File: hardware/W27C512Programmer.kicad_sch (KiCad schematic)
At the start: 104 parts, among them J1 CTRL, J2 MSB, J3 LSB, J4 Ext_UART, J5 OLED, J6 VP, J7 SAO, Q1 MMBT3904, Q2 MMBT3906, Q3 MMBT3904, Q4 MMBT3904, Q5 MMBT3904, Q6 MMBT3906, Q7 MMBT3906, Q8 MMBT3906, SW1 RST, SW2 USR, U1 MIC2288, U2 74HC573, U3 74HC573, U4 74HC573, U5 28/32 pin ROM

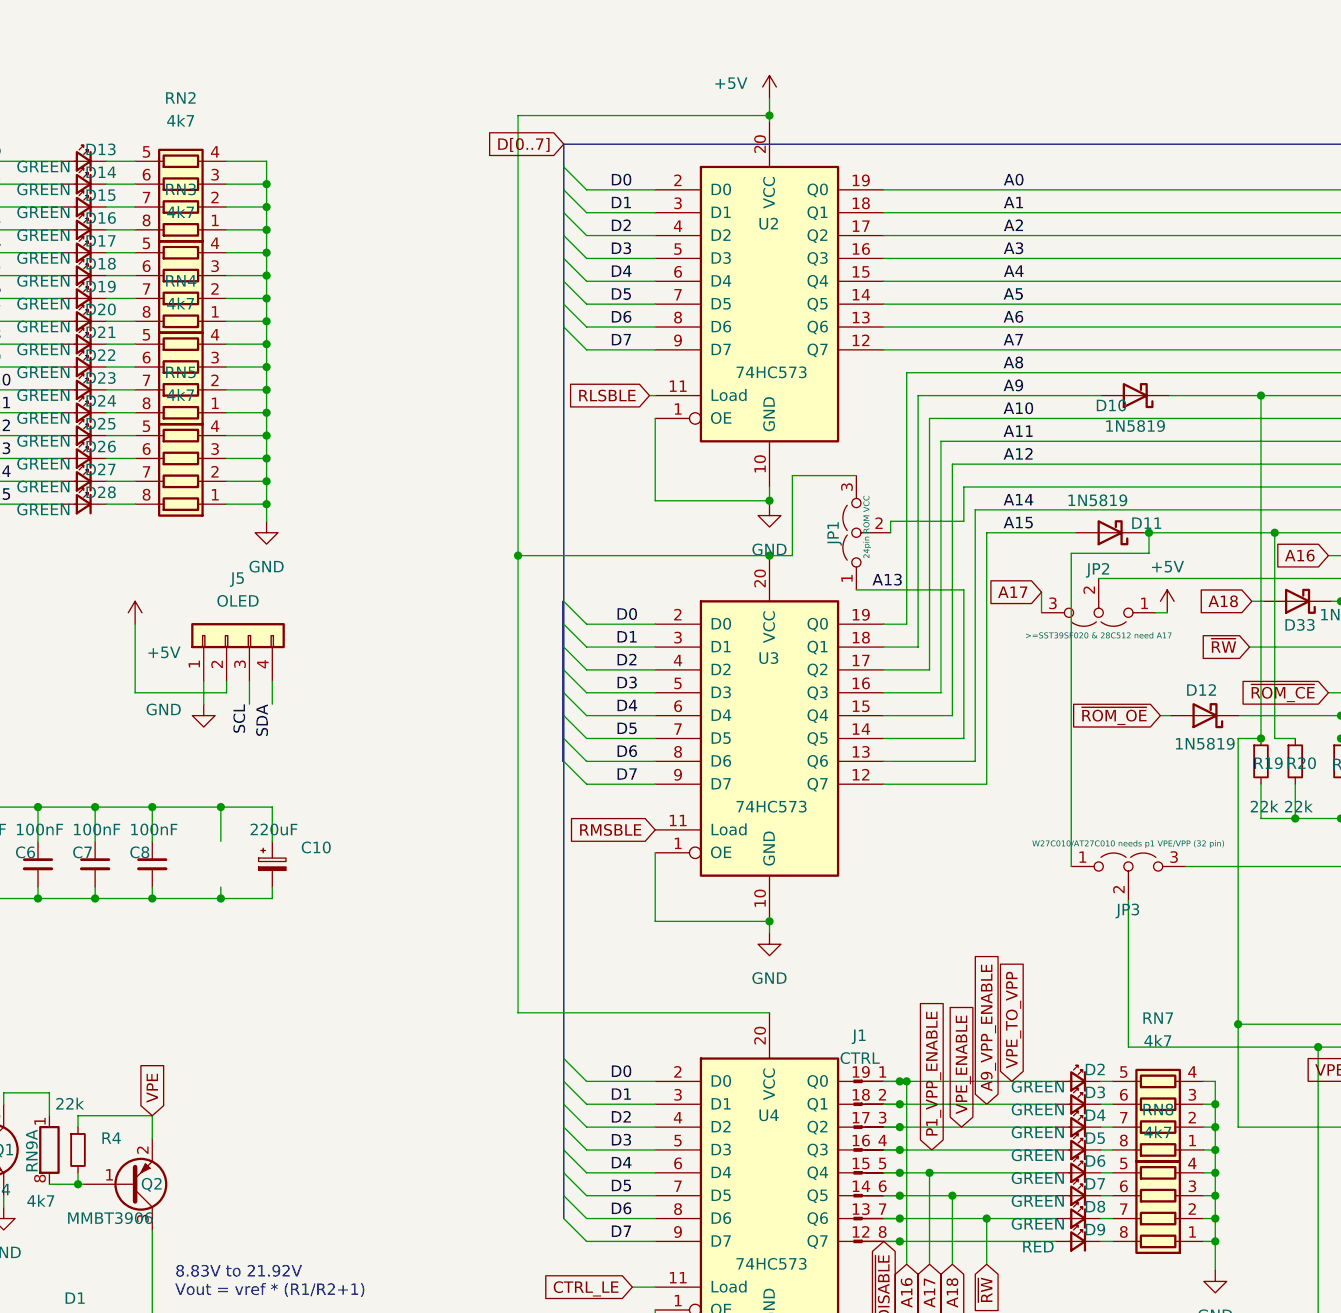
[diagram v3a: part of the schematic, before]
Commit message: Change 4k7 to 10k R for green LEDs
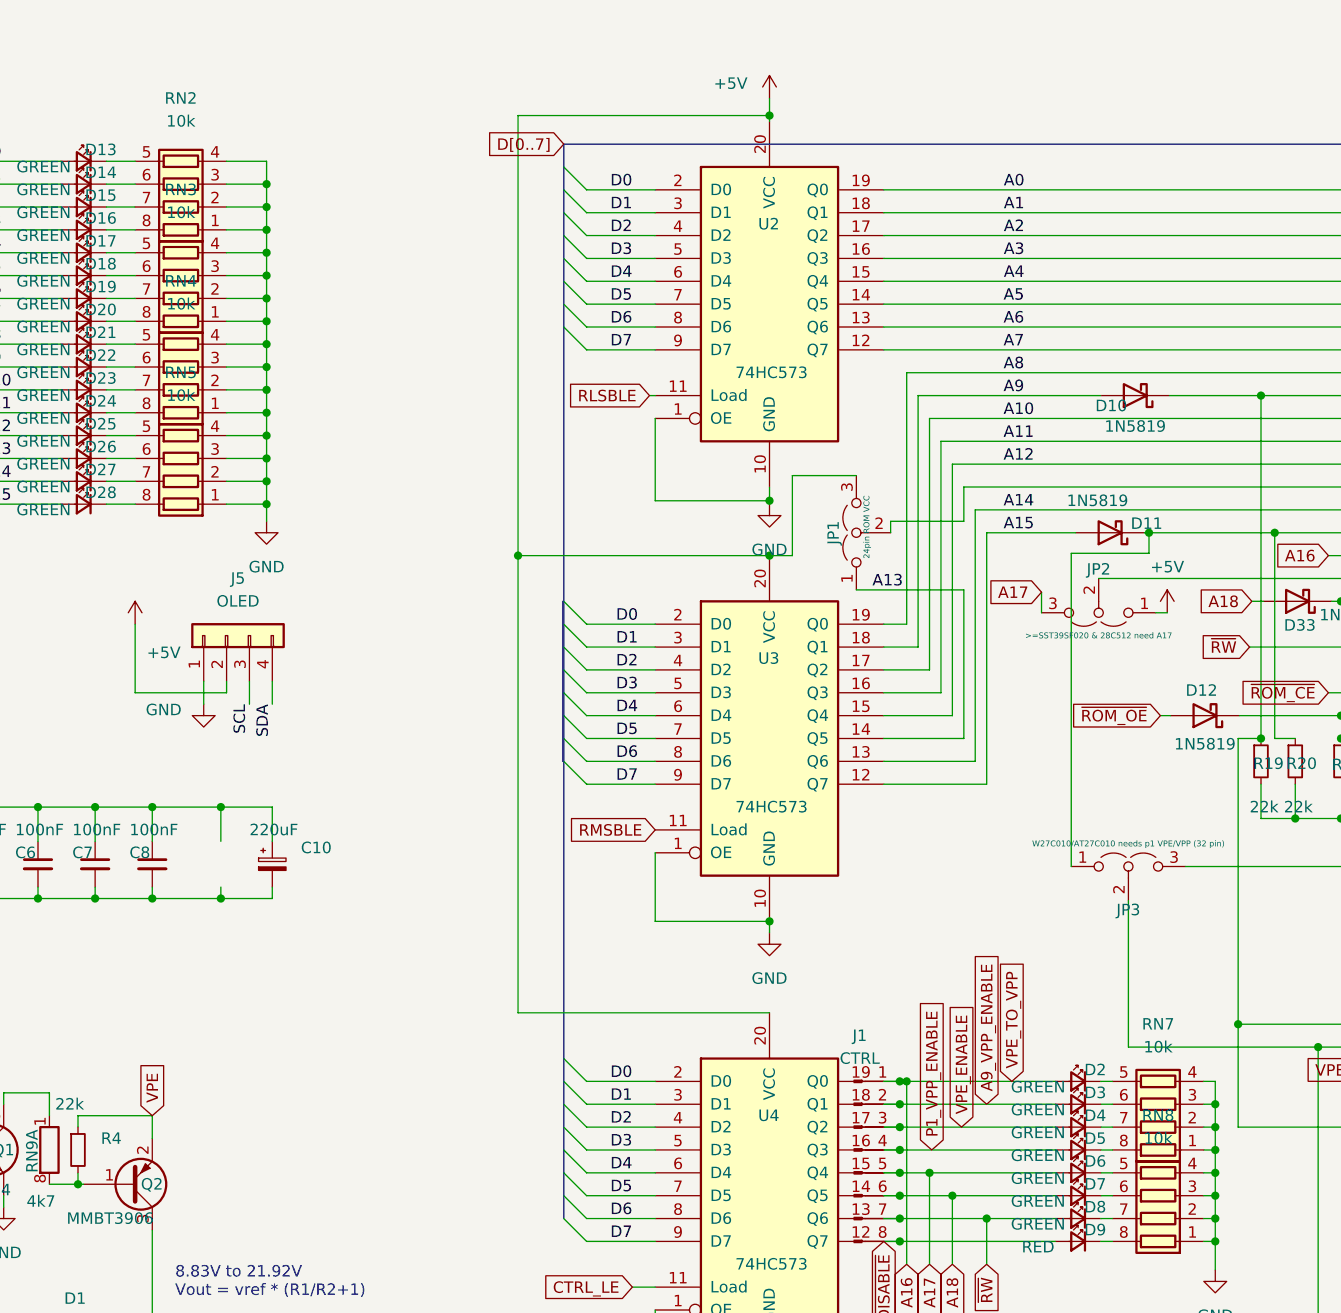
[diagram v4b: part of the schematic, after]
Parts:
- RN2, RN3, RN4, RN5, RN7, RN8: value 4k7 -> 10k
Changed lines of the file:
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@@
     (in_bom yes) (on_board yes) (fields_autoplaced)
     (property "Reference" "RN5" (id 0) (at 65.405 48.26 90))
-    (property "Value" "4k7" (id 1) (at 65.405 50.8 90))
+    (property "Value" "10k" (id 1) (at 65.405 50.8 90))
     (property "Footprint" "Resistor_SMD:R_Array_Convex_4x0603" (id 2) (at 65.405 50.8 90)
       (effects (font (size 1.27 1.27)) hide)
@@
   (symbol (lib_id "Device:R_Pack04") (at 173.99 129.54 90) (unit 1)
     (in_bom yes) (on_board yes) (fields_autoplaced)
-    (property "Reference" "RN7" (id 0) (at 173.99 120.015 90))
-    (property "Value" "4k7" (id 1) (at 173.99 122.555 90))
+    (property "Reference" "RN7" (id 0) (at 173.99 120.65 90))
+    (property "Value" "10k" (id 1) (at 173.99 123.19 90))
     (property "Footprint" "Resistor_SMD:R_Array_Convex_4x0603" (id 2) (at 173.99 122.555 90)
       (effects (font (size 1.27 1.27)) hide)
@@
     (in_bom yes) (on_board yes) (fields_autoplaced)
     (property "Reference" "RN2" (id 0) (at 65.405 17.78 90))
-    (property "Value" "4k7" (id 1) (at 65.405 20.32 90))
+    (property "Value" "10k" (id 1) (at 65.405 20.32 90))
     (property "Footprint" "Resistor_SMD:R_Array_Convex_4x0603" (id 2) (at 65.405 20.32 90)
       (effects (font (size 1.27 1.27)) hide)
@@
     (in_bom yes) (on_board yes) (fields_autoplaced)
     (property "Reference" "RN4" (id 0) (at 65.405 38.1 90))
-    (property "Value" "4k7" (id 1) (at 65.405 40.64 90))
+    (property "Value" "10k" (id 1) (at 65.405 40.64 90))
     (property "Footprint" "Resistor_SMD:R_Array_Convex_4x0603" (id 2) (at 65.405 40.64 90)
       (effects (font (size 1.27 1.27)) hide)
@@
   (symbol (lib_id "Device:R_Pack04") (at 173.99 139.7 90) (unit 1)
     (in_bom yes) (on_board yes) (fields_autoplaced)
-    (property "Reference" "RN8" (id 0) (at 173.99 130.175 90))
-    (property "Value" "4k7" (id 1) (at 173.99 132.715 90))
+    (property "Reference" "RN8" (id 0) (at 173.99 130.81 90))
+    (property "Value" "10k" (id 1) (at 173.99 133.35 90))
     (property "Footprint" "Resistor_SMD:R_Array_Convex_4x0603" (id 2) (at 173.99 132.715 90)
       (effects (font (size 1.27 1.27)) hide)
@@
     (in_bom yes) (on_board yes) (fields_autoplaced)
     (property "Reference" "RN3" (id 0) (at 65.405 27.94 90))
-    (property "Value" "4k7" (id 1) (at 65.405 30.48 90))
+    (property "Value" "10k" (id 1) (at 65.405 30.48 90))
     (property "Footprint" "Resistor_SMD:R_Array_Convex_4x0603" (id 2) (at 65.405 30.48 90)
       (effects (font (size 1.27 1.27)) hide)
@@
     )
     (path "/227471f3-86b6-42ab-a5c2-bb8c27f54d78"
-      (reference "RN2") (unit 1) (value "4k7") (footprint "Resistor_SMD:R_Array_Convex_4x0603")
+      (reference "RN2") (unit 1) (value "10k") (footprint "Resistor_SMD:R_Array_Convex_4x0603")
     )
     (path "/d3905eaa-b1c1-4bb1-bcd5-eb92ab43f325"
-      (reference "RN3") (unit 1) (value "4k7") (footprint "Resistor_SMD:R_Array_Convex_4x0603")
+      (reference "RN3") (unit 1) (value "10k") (footprint "Resistor_SMD:R_Array_Convex_4x0603")
     )
     (path "/7d885514-66e1-4cc3-90c0-754d7a0aafdb"
-      (reference "RN4") (unit 1) (value "4k7") (footprint "Resistor_SMD:R_Array_Convex_4x0603")
+      (reference "RN4") (unit 1) (value "10k") (footprint "Resistor_SMD:R_Array_Convex_4x0603")
     )
     (path "/04dd25b6-9c7a-4ba6-835d-4334cbe2cee8"
-      (reference "RN5") (unit 1) (value "4k7") (footprint "Resistor_SMD:R_Array_Convex_4x0603")
+      (reference "RN5") (unit 1) (value "10k") (footprint "Resistor_SMD:R_Array_Convex_4x0603")
     )
     (path "/0f501c02-0a9a-464e-8af2-de796bd02d4b"
-      (reference "RN7") (unit 1) (value "4k7") (footprint "Resistor_SMD:R_Array_Convex_4x0603")
+      (reference "RN7") (unit 1) (value "10k") (footprint "Resistor_SMD:R_Array_Convex_4x0603")
     )
     (path "/81aff399-6a94-4636-923b-284fbe940fdd"
-      (reference "RN8") (unit 1) (value "4k7") (footprint "Resistor_SMD:R_Array_Convex_4x0603")
+      (reference "RN8") (unit 1) (value "10k") (footprint "Resistor_SMD:R_Array_Convex_4x0603")
     )
     (path "/14c48f03-3857-4481-b7ff-b9662e4ca09d"

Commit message: 10k LED R
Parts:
- RN2, RN3, RN4, RN5, RN7, RN8: LCSC C1980 -> C29718
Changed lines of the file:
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@@
       (effects (font (size 1.27 1.27)) hide)
     )
-    (property "LCSC" "C1980" (id 4) (at 65.405 57.785 0)
+    (property "LCSC" "C29718" (id 4) (at 65.405 57.785 0)
       (effects (font (size 1.27 1.27)) hide)
     )
@@
       (effects (font (size 1.27 1.27)) hide)
     )
-    (property "LCSC" "C1980" (id 4) (at 173.99 129.54 0)
+    (property "LCSC" "C29718" (id 4) (at 173.99 129.54 0)
       (effects (font (size 1.27 1.27)) hide)
     )
@@
       (effects (font (size 1.27 1.27)) hide)
     )
-    (property "LCSC" "C1980" (id 4) (at 65.405 27.305 0)
+    (property "LCSC" "C29718" (id 4) (at 65.405 27.305 0)
       (effects (font (size 1.27 1.27)) hide)
     )
@@
       (effects (font (size 1.27 1.27)) hide)
     )
-    (property "LCSC" "C1980" (id 4) (at 65.405 47.625 0)
+    (property "LCSC" "C29718" (id 4) (at 65.405 47.625 0)
       (effects (font (size 1.27 1.27)) hide)
     )
@@
       (effects (font (size 1.27 1.27)) hide)
     )
-    (property "LCSC" "C1980" (id 4) (at 173.99 139.7 0)
+    (property "LCSC" "C29718" (id 4) (at 173.99 139.7 0)
       (effects (font (size 1.27 1.27)) hide)
     )
@@
       (effects (font (size 1.27 1.27)) hide)
     )
-    (property "LCSC" "C1980" (id 4) (at 65.405 37.465 0)
-      (effects (font (size 1.27 1.27)) hide)
-    )
+    (property "LCSC" "C29718" (id 4) (at 65.405 37.465 0)
+      (effects (font (size 1.27 1.27)) hide)
+    )

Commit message: Fiddle with pin naming
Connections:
- net P1_VPP_ENABLE is gone; now on net A18: D5.2 (A), J1.4 (Pin_4), R25.1, U4.16 (Q3)
- net A16: now also D7.2 (A), J1.6 (Pin_6), U4.14 (Q5); no longer D2.2 (A), J1.1 (Pin_1), R2.1, U4.19 (Q0)
- net A18: no longer D7.2 (A), J1.6 (Pin_6), U4.14 (Q5)
- net ~{RW} renamed P31
- new net VPE_TO_VPP: D2.2 (A), J1.1 (Pin_1), R2.1, U4.19 (Q0)
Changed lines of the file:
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@@
   (junction (at 74.93 62.865) (diameter 0) (color 0 0 0 0)
   )
-  (junction (at 146.05 127) (diameter 0) (color 0 0 0 0)
-  )
   (junction (at 185.42 50.8) (diameter 0) (color 0 0 0 0)
   )
@@
   )
   (junction (at 74.93 32.385) (diameter 0) (color 0 0 0 0)
+  )
+  (junction (at 160.655 162.687) (diameter 0) (color 0 0 0 0)
   )
   (junction (at 194.31 97.79) (diameter 0) (color 0 0 0 0)
@@
     (stroke (width 0) (type default) (color 0 0 0 0))
   )
+  (wire (pts (xy 160.655 156.591) (xy 157.607 156.591))
+    (stroke (width 0) (type default) (color 0 0 0 0))
+  )
   (wire (pts (xy 49.53 96.52) (xy 55.88 96.52))
     (stroke (width 0) (type default) (color 0 0 0 0))
@@
     (stroke (width 0) (type default) (color 0 0 0 0))
   )
-  (wire (pts (xy 146.05 127) (xy 162.56 127))
+  (wire (pts (xy 145.288 127) (xy 162.56 127))
     (stroke (width 0) (type default) (color 0 0 0 0))
   )
@@
     (stroke (width 0) (type default) (color 0 0 0 0))
   )
+  (wire (pts (xy 157.353 159.512) (xy 162.687 159.512))
+    (stroke (width 0) (type default) (color 0 0 0 0))
+  )
   (wire (pts (xy 276.86 144.78) (xy 267.97 144.78))
     (stroke (width 0) (type default) (color 0 0 0 0))
@@
     (stroke (width 0) (type default) (color 0 0 0 0))
   )
+  (wire (pts (xy 158.623 172.72) (xy 162.433 172.72))
+    (stroke (width 0) (type default) (color 0 0 0 0))
+  )
   (wire (pts (xy 34.925 32.385) (xy 52.07 32.385))
     (stroke (width 0) (type default) (color 0 0 0 0))
@@
     (stroke (width 0) (type default) (color 0 0 0 0))
   )
-  (wire (pts (xy 145.288 127) (xy 146.05 127))
-    (stroke (width 0) (type default) (color 0 0 0 0))
-  )
   (wire (pts (xy 55.88 106.68) (xy 62.23 106.68))
     (stroke (width 0) (type default) (color 0 0 0 0))
@@
     (stroke (width 0) (type default) (color 0 0 0 0))
   )
+  (wire (pts (xy 160.655 162.687) (xy 162.687 162.687))
+    (stroke (width 0) (type default) (color 0 0 0 0))
+  )
   (wire (pts (xy 49.53 105.41) (xy 49.53 106.68))
     (stroke (width 0) (type default) (color 0 0 0 0))
@@
     (stroke (width 0) (type default) (color 0 0 0 0))
   )
+  (wire (pts (xy 158.877 166.243) (xy 162.56 166.243))
+    (stroke (width 0) (type default) (color 0 0 0 0))
+  )
   (wire (pts (xy 241.3 91.44) (xy 242.57 91.44))
     (stroke (width 0) (type default) (color 0 0 0 0))
@@
     (stroke (width 0) (type default) (color 0 0 0 0))
   )
+  (wire (pts (xy 160.655 162.687) (xy 160.655 156.591))
+    (stroke (width 0) (type default) (color 0 0 0 0))
+  )
   (wire (pts (xy 74.93 50.165) (xy 74.93 52.705))
     (stroke (width 0) (type default) (color 0 0 0 0))
@@
     (stroke (width 0) (type default) (color 0 0 0 0))
   )
+  (wire (pts (xy 158.496 162.687) (xy 160.655 162.687))
+    (stroke (width 0) (type default) (color 0 0 0 0))
+  )
   (wire (pts (xy 110.49 78.74) (xy 118.11 78.74))
     (stroke (width 0) (type default) (color 0 0 0 0))
@@
   )
   (wire (pts (xy 267.97 125.73) (xy 269.24 125.73))
-    (stroke (width 0) (type default) (color 0 0 0 0))
-  )
-  (wire (pts (xy 146.05 127) (xy 146.05 147.32))
     (stroke (width 0) (type default) (color 0 0 0 0))
   )
@@
     )
   )
-  (global_label "A18" (shape input) (at 151.13 147.32 270) (fields_autoplaced)
-    (effects (font (size 1.27 1.27)) (justify right))
-    (property "Intersheet References" "${INTERSHEET_REFS}" (id 0) (at 151.0506 153.2407 90)
+  (global_label "P2" (shape input) (at 151.13 147.32 270) (fields_autoplaced)
+    (effects (font (size 1.27 1.27)) (justify right))
+    (property "Intersheet References" "${INTERSHEET_REFS}" (id 0) (at 151.0506 152.1237 90)
       (effects (font (size 1.27 1.27)) (justify right) hide)
     )
@@
     )
   )
-  (global_label "A17" (shape input) (at 148.59 147.32 270) (fields_autoplaced)
-    (effects (font (size 1.27 1.27)) (justify right))
-    (property "Intersheet References" "${INTERSHEET_REFS}" (id 0) (at 148.5106 153.2407 90)
+  (global_label "P30" (shape input) (at 148.59 147.32 270) (fields_autoplaced)
+    (effects (font (size 1.27 1.27)) (justify right))
+    (property "Intersheet References" "${INTERSHEET_REFS}" (id 0) (at 148.5106 153.3332 90)
       (effects (font (size 1.27 1.27)) (justify right) hide)
     )
@@
     )
   )
+  (global_label "P2" (shape input) (at 157.353 159.512 180) (fields_autoplaced)
+    (effects (font (size 1.27 1.27)) (justify right))
+    (property "Intersheet References" "${INTERSHEET_REFS}" (id 0) (at 152.5493 159.4326 0)
+      (effects (font (size 1.27 1.27)) (justify right) hide)
+    )
+  )
   (global_label "~{ROM_OE}" (shape input) (at 240.03 53.34 180) (fields_autoplaced)
     (effects (font (size 1.27 1.27)) (justify right))
@@
     (effects (font (size 1.27 1.27)) (justify right))
     (property "Intersheet References" "${INTERSHEET_REFS}" (id 0) (at 178.4833 73.5806 0)
+      (effects (font (size 1.27 1.27)) (justify right) hide)
+    )
+  )
+  (global_label "P1_VPP_ENABLE" (shape input) (at 158.496 162.687 180) (fields_autoplaced)
+    (effects (font (size 1.27 1.27)) (justify right))
+    (property "Intersheet References" "${INTERSHEET_REFS}" (id 0) (at 141.0243 162.7664 0)
       (effects (font (size 1.27 1.27)) (justify right) hide)
     )
@@
     )
   )
+  (global_label "~{RW}" (shape input) (at 162.56 166.243 0) (fields_autoplaced)
+    (effects (font (size 1.27 1.27)) (justify left))
+    (property "Intersheet References" "${INTERSHEET_REFS}" (id 0) (at 167.6945 166.3224 0)
+      (effects (font (size 1.27 1.27)) (justify left) hide)
+    )
+  )
   (global_label "VPE_ENABLE" (shape input) (at 241.3 91.44 180) (fields_autoplaced)
     (effects (font (size 1.27 1.27)) (justify right))
@@
     )
   )
+  (global_label "A17" (shape input) (at 162.433 172.72 0) (fields_autoplaced)
+    (effects (font (size 1.27 1.27)) (justify left))
+    (property "Intersheet References" "${INTERSHEET_REFS}" (id 0) (at 168.3537 172.7994 0)
+      (effects (font (size 1.27 1.27)) (justify left) hide)
+    )
+  )
   (global_label "CTRL_LE" (shape input) (at 240.03 55.88 180) (fields_autoplaced)
     (effects (font (size 1.27 1.27)) (justify right))
     (property "Intersheet References" "${INTERSHEET_REFS}" (id 0) (at 229.9364 55.8006 0)
+      (effects (font (size 1.27 1.27)) (justify right) hide)
+    )
+  )
+  (global_label "P31" (shape input) (at 158.877 166.243 180) (fields_autoplaced)
+    (effects (font (size 1.27 1.27)) (justify right))
+    (property "Intersheet References" "${INTERSHEET_REFS}" (id 0) (at 152.8638 166.1636 0)
       (effects (font (size 1.27 1.27)) (justify right) hide)
     )
@@
     )
   )
-  (global_label "~{RW}" (shape input) (at 154.94 147.32 270) (fields_autoplaced)
-    (effects (font (size 1.27 1.27)) (justify right))
-    (property "Intersheet References" "${INTERSHEET_REFS}" (id 0) (at 154.8606 152.4545 90)
+  (global_label "P31" (shape input) (at 154.94 147.32 270) (fields_autoplaced)
+    (effects (font (size 1.27 1.27)) (justify right))
+    (property "Intersheet References" "${INTERSHEET_REFS}" (id 0) (at 154.8606 153.3332 90)
       (effects (font (size 1.27 1.27)) (justify right) hide)
     )
@@
     (property "Intersheet References" "${INTERSHEET_REFS}" (id 0) (at 308.61 104.14 0)
       (effects (font (size 1.27 1.27)) hide)
+    )
+  )
+  (global_label "P30" (shape input) (at 158.623 172.72 180) (fields_autoplaced)
+    (effects (font (size 1.27 1.27)) (justify right))
+    (property "Intersheet References" "${INTERSHEET_REFS}" (id 0) (at 152.6098 172.6406 0)
+      (effects (font (size 1.27 1.27)) (justify right) hide)
     )
   )
@@
     )
   )
+  (global_label "A18" (shape input) (at 162.687 162.687 0) (fields_autoplaced)
+    (effects (font (size 1.27 1.27)) (justify left))
+    (property "Intersheet References" "${INTERSHEET_REFS}" (id 0) (at 168.6077 162.7664 0)
+      (effects (font (size 1.27 1.27)) (justify left) hide)
+    )
+  )
+  (global_label "P1" (shape input) (at 157.607 156.591 180) (fields_autoplaced)
+    (effects (font (size 1.27 1.27)) (justify right))
+    (property "Intersheet References" "${INTERSHEET_REFS}" (id 0) (at 152.8033 156.5116 0)
+      (effects (font (size 1.27 1.27)) (justify right) hide)
+    )
+  )
   (global_label "RMSBLE" (shape input) (at 118.11 99.06 180) (fields_autoplaced)
     (effects (font (size 1.27 1.27)) (justify right))
@@
     )
   )
-  (global_label "A16" (shape input) (at 146.05 147.32 270) (fields_autoplaced)
-    (effects (font (size 1.27 1.27)) (justify right))
-    (property "Intersheet References" "${INTERSHEET_REFS}" (id 0) (at 145.9706 153.2407 90)
-      (effects (font (size 1.27 1.27)) (justify right) hide)
-    )
-  )
+  (global_label "A16" (shape input) (at 162.687 159.512 0) (fields_autoplaced)
+    (effects (font (size 1.27 1.27)) (justify left))
+    (property "Intersheet References" "${INTERSHEET_REFS}" (id 0) (at 168.6077 159.5914 0)
+      (effects (font (size 1.27 1.27)) (justify left) hide)
+    )
+  )
